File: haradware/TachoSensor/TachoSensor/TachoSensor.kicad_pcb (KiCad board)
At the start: 2 copper layers, 30 x 15 mm, 6 parts, among them J101 OUT

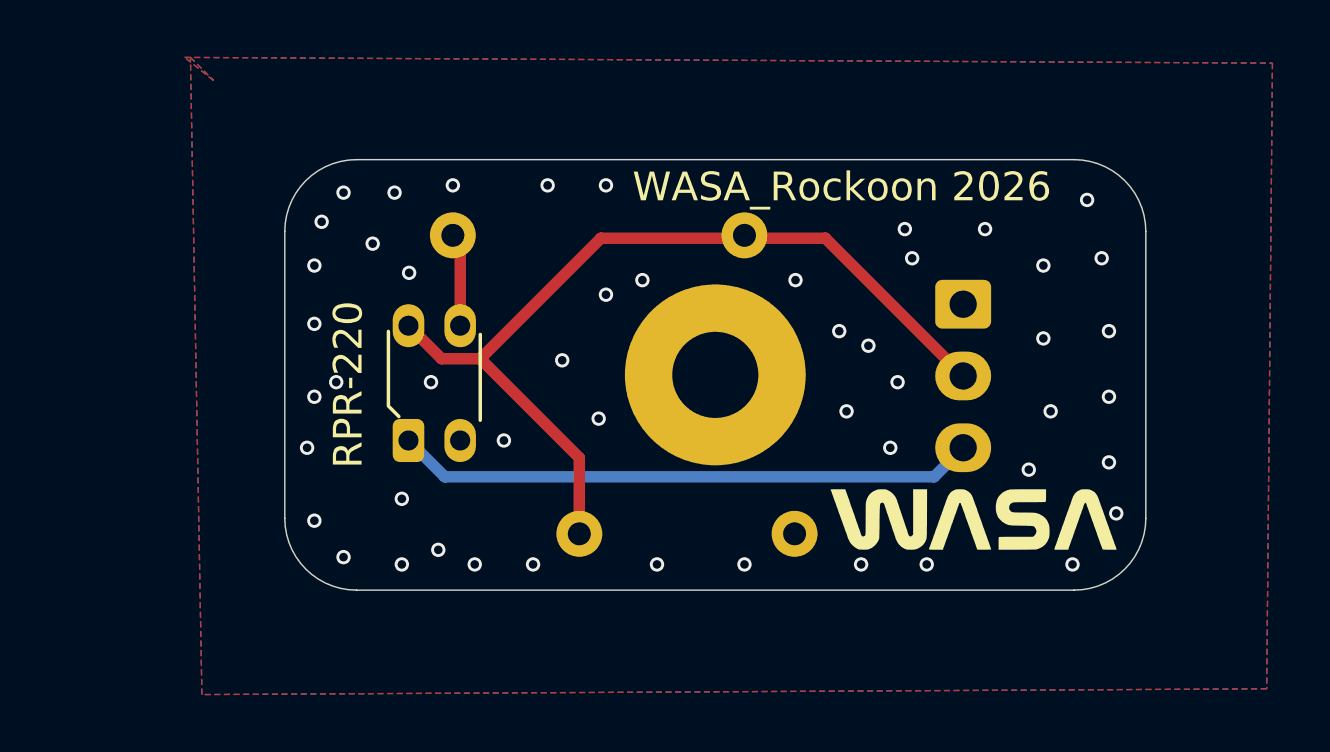
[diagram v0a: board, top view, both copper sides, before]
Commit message: シルク追加してガーバー出力
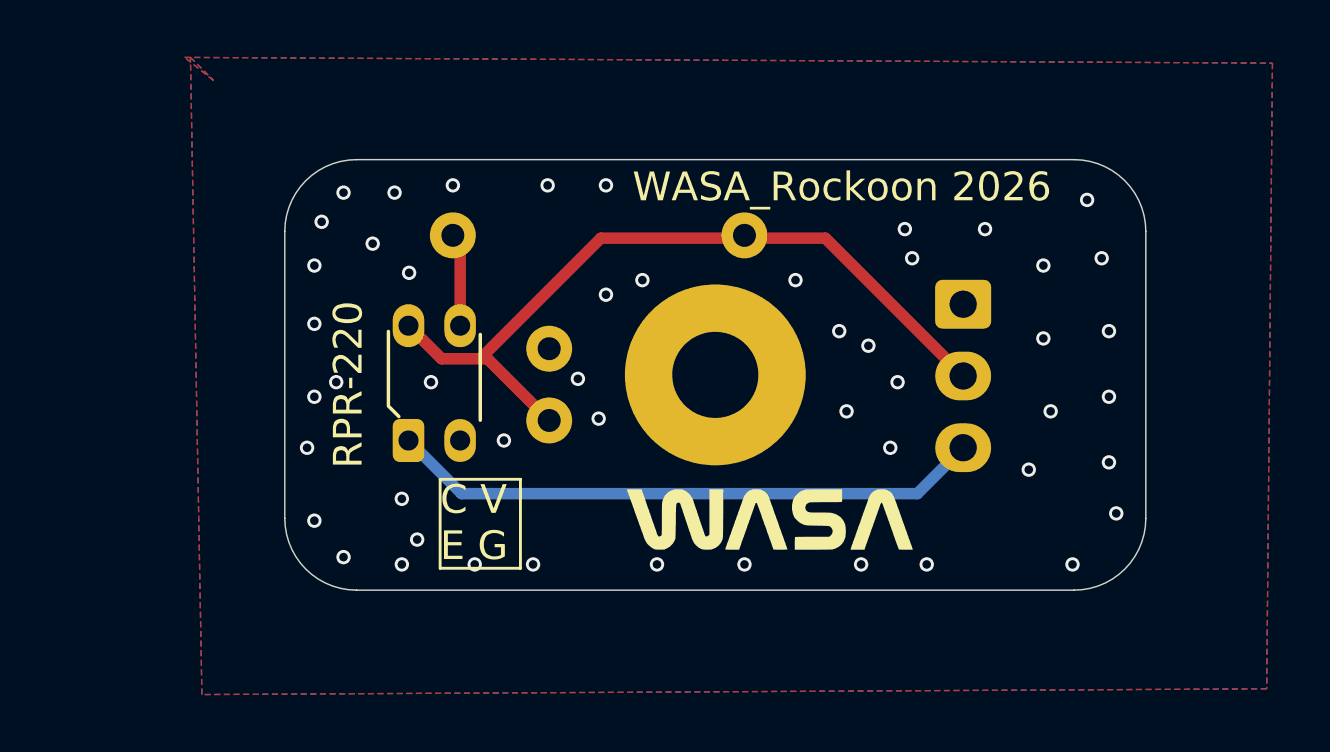
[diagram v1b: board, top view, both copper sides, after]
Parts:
- 0.1uF: renamed from C101; footprint Capacitor_THT:C_Axial_L3.8mm_D2.6mm_P7.50mm_Horizontal -> Capacitor_THT:C_Disc_D5.0mm_W2.5mm_P2.50mm
- moved G*** 7.10 mm to (159.9, 94.7)
- moved 0.1uF 4.09 mm to (152.2, 91.2), turned to 90 degrees
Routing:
- net Net-(J101-Pin_2): track 31.1 -> 26.8 mm
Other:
- board text added: "C V E G"
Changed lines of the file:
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@@
 				(font
 					(size 1 1)
-					(thickness 0.15)
+					(thickness 0.125)
 				)
 			)
@@
 	(footprint "Library:wasa_10mm"
 		(layer "F.Cu")
-		(at 167 94.7)
+		(at 159.9 94.7)
 		(property "Reference" "G***"
 			(at 0.108168 3.048 0)
@@
 		(embedded_fonts no)
 	)
-	(footprint "Capacitor_THT:C_Axial_L3.8mm_D2.6mm_P7.50mm_Horizontal"
+	(footprint "Capacitor_THT:C_Disc_D5.0mm_W2.5mm_P2.50mm"
 		(layer "B.Cu")
-		(at 153.25 95.2)
-		(descr "C, Axial series, Axial, Horizontal, pin pitch=7.5mm, length*diameter=3.8*2.6mm^2, http://www.vishay.com/docs/45231/arseries.pdf")
-		(tags "C Axial series Axial Horizontal pin pitch 7.5mm  length 3.8mm diameter 2.6mm")
-		(property "Reference" "C101"
-			(at 3.85 6.1 0)
+		(at 152.2 91.25 90)
+		(descr "C, Disc series, Radial, pin pitch=2.50mm, diameter*width=5*2.5mm^2, Capacitor, http://cdn-reichelt.de/documents/datenblatt/B300/DS_KERKO_TC.pdf")
+		(tags "C Disc series Radial pin pitch 2.50mm diameter 5mm width 2.5mm Capacitor")
+		(property "Reference" "0.1uF"
+			(at -3.55 -0.2 90)
 			(layer "B.SilkS")
 			(effects
@@
 		)
 		(property "Value" "0.1uF"
-			(at 3.75 0.1 0)
-			(layer "B.SilkS")
+			(at 1.25 -2.5 90)
+			(layer "B.Fab")
 			(effects
 				(font
@@
 		)
 		(property "Datasheet" "~"
-			(at 0 0 0)
+			(at 0 0 90)
 			(layer "B.Fab")
 			(hide yes)
@@
 		)
 		(property "Description" "Unpolarized capacitor"
-			(at 0 0 0)
+			(at 0 0 90)
 			(layer "B.Fab")
 			(hide yes)
@@
 		(attr through_hole)
 		(fp_line
-			(start 1.04 0)
-			(end 1.73 0)
-			(stroke
-				(width 0.12)
-				(type solid)
-			)
-			(layer "B.SilkS")
-		)
-		(fp_line
-			(start 6.46 0)
-			(end 5.77 0)
+			(start 3.87 -1.37)
+			(end -1.37 -1.37)
+			(stroke
+				(width 0.12)
+				(type solid)
+			)
+			(layer "B.SilkS")
+		)
+		(fp_line
+			(start -1.37 -1.37)
+			(end -1.37 1.37)
+			(stroke
+				(width 0.12)
+				(type solid)
+			)
+			(layer "B.SilkS")
+		)
+		(fp_line
+			(start 3.87 1.37)
+			(end 3.87 -1.37)
+			(stroke
+				(width 0.12)
+				(type solid)
+			)
+			(layer "B.SilkS")
+		)
+		(fp_line
+			(start -1.37 1.37)
+			(end 3.87 1.37)
 			(stroke
 				(width 0.12)
@@
 		)
 		(fp_rect
-			(start 1.73 1.42)
-			(end 5.77 -1.42)
-			(stroke
-				(width 0.12)
-				(type solid)
-			)
-			(fill no)
-			(layer "B.SilkS")
-		)
-		(fp_rect
-			(start -1.05 1.55)
-			(end 8.55 -1.55)
+			(start -1.5 1.5)
+			(end 4 -1.5)
 			(stroke
 				(width 0.05)
@@
 			(layer "B.CrtYd")
 		)
-		(fp_line
-			(start 0 0)
-			(end 1.85 0)
-			(stroke
-				(width 0.1)
-				(type solid)
-			)
-			(layer "B.Fab")
-		)
-		(fp_line
-			(start 7.5 0)
-			(end 5.65 0)
-			(stroke
-				(width 0.1)
-				(type solid)
-			)
-			(layer "B.Fab")
-		)
 		(fp_rect
-			(start 1.85 1.3)
-			(end 5.65 -1.3)
+			(start -1.25 1.25)
+			(end 3.75 -1.25)
 			(stroke
 				(width 0.1)
@@
 		)
 		(fp_text user "${REFERENCE}"
-			(at 3.75 0 0)
-			(layer "B.Fab")
-			(effects
-				(font
-					(size 0.76 0.76)
-					(thickness 0.114)
+			(at 1.25 0 90)
+			(layer "B.Fab")
+			(effects
+				(font
+					(size 1 1)
+					(thickness 0.15)
 				)
 				(justify mirror)
@@
 		)
 		(pad "1" thru_hole circle
-			(at 0 0)
+			(at 0 0 90)
 			(size 1.6 1.6)
 			(drill 0.8)
@@
 		)
 		(pad "2" thru_hole circle
-			(at 7.5 0)
+			(at 2.5 0 90)
 			(size 1.6 1.6)
 			(drill 0.8)
@@
 		)
 		(embedded_fonts no)
-		(model "${KICAD9_3DMODEL_DIR}/Capacitor_THT.3dshapes/C_Axial_L3.8mm_D2.6mm_P7.50mm_Horizontal.step"
+		(model "${KICAD9_3DMODEL_DIR}/Capacitor_THT.3dshapes/C_Disc_D5.0mm_W2.5mm_P2.50mm.step"
 			(offset
 				(xyz 0 0 0)
@@
 		)
 	)
+	(gr_rect
+		(start 148.4 93.3)
+		(end 151.2 96.4)
+		(stroke
+			(width 0.1)
+			(type default)
+		)
+		(fill no)
+		(layer "F.SilkS")
+	)
 	(gr_text "WASA_Rockoon 2026\n"
 		(at 155.1 83.7 0)
@@
 		)
 	)
+	(gr_text "C V\nE G"
+		(at 148.4 96.2 0)
+		(layer "F.SilkS")
+		(effects
+			(font
+				(size 1 1)
+				(thickness 0.1)
+			)
+			(justify left bottom)
+		)
+	)
 	(gr_text "TachoSensor\n"
 		(at 170.974 83.9 0)
@@
 	)
 	(segment
-		(start 153.25 95.2)
-		(end 153.25 92.548)
-		(width 0.4)
-		(layer "F.Cu")
-		(net 1)
-	)
-	(segment
 		(start 147.298 87.948)
 		(end 148.449 89.099)
@@
 	)
 	(segment
-		(start 153.25 92.548)
-		(end 149.801 89.099)
+		(start 149.801 89.099)
+		(end 150.049 89.099)
 		(width 0.4)
 		(layer "F.Cu")
@@
 		(net 1)
 	)
+	(segment
+		(start 150.049 89.099)
+		(end 152.2 91.25)
+		(width 0.4)
+		(layer "F.Cu")
+		(net 1)
+	)
 	(via
 		(at 169.418 85.852)
@@
 	)
 	(via
-		(at 148.336 95.758)
+		(at 147.6 95.4)
 		(size 0.5)
 		(drill 0.3)
@@
 	)
 	(via
-		(at 152.654 89.154)
+		(at 153.2 89.8)
 		(size 0.5)
 		(drill 0.3)
@@
 	)
 	(segment
-		(start 147.298 91.948)
-		(end 148.563 93.213)
+		(start 165.024 93.8)
+		(end 166.624 92.2)
 		(width 0.4)
 		(layer "B.Cu")
@@
 	)
 	(segment
-		(start 148.563 93.213)
-		(end 165.611 93.213)
+		(start 149.15 93.8)
+		(end 165.024 93.8)
 		(width 0.4)
 		(layer "B.Cu")
@@
 	)
 	(segment
-		(start 165.611 93.213)
-		(end 166.624 92.2)
+		(start 147.298 91.948)
+		(end 149.15 93.8)
 		(width 0.4)
 		(layer "B.Cu")

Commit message: SMDタイプの設計．PWRLEDを追加
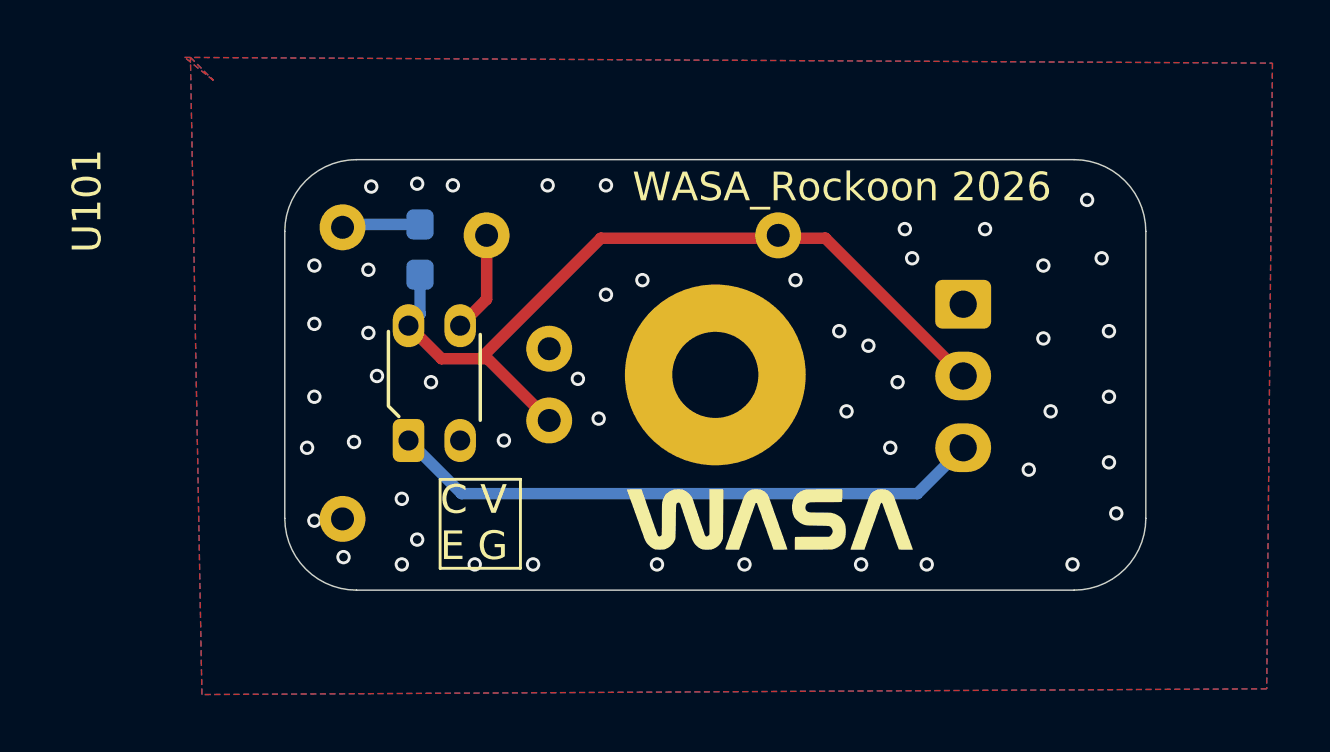
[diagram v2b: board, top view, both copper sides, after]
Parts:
- added D101: PWR, LED_SMD:LED_0603_1608Metric_Pad1.05x0.95mm_HandSolder, B.Cu at (147.7, 85.3)
- added R102: 1k, Resistor_THT:R_Axial_DIN0207_L6.3mm_D2.5mm_P10.16mm_Horizontal, B.Cu at (145.0, 84.5)
- R101: value 100Ω -> 100
- moved R101 1.18 mm to (150.0, 84.8)
- renumbered RPR-220 to U101
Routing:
- net Net-(D101-K): track 0.00 -> 2.74 mm
- net Net-(D101-A): track 26.8 -> 28.8 mm
